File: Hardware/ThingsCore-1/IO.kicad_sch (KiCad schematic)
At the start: 9 parts, among them U7 STM32MP133DAE7, Y1 X322516MLB4SI, Y2 Q13FC13500004

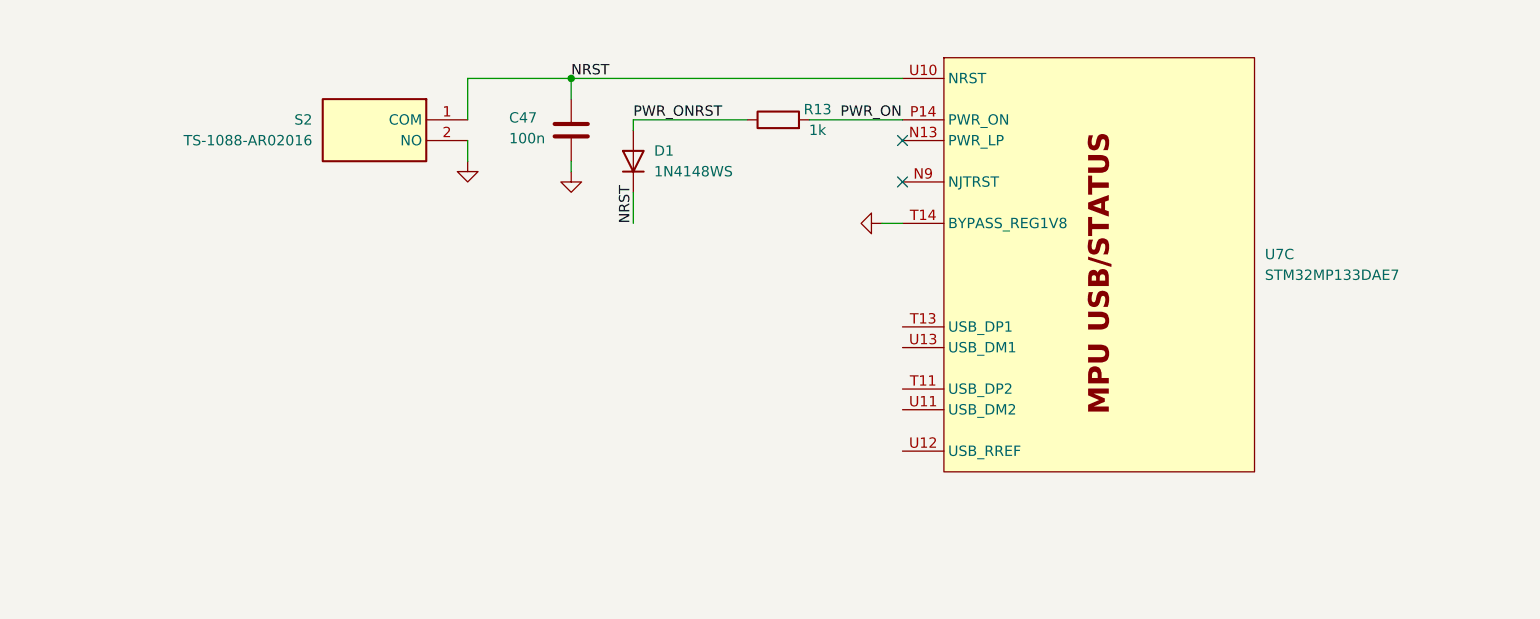
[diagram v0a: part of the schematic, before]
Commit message: ddr3 fanout done
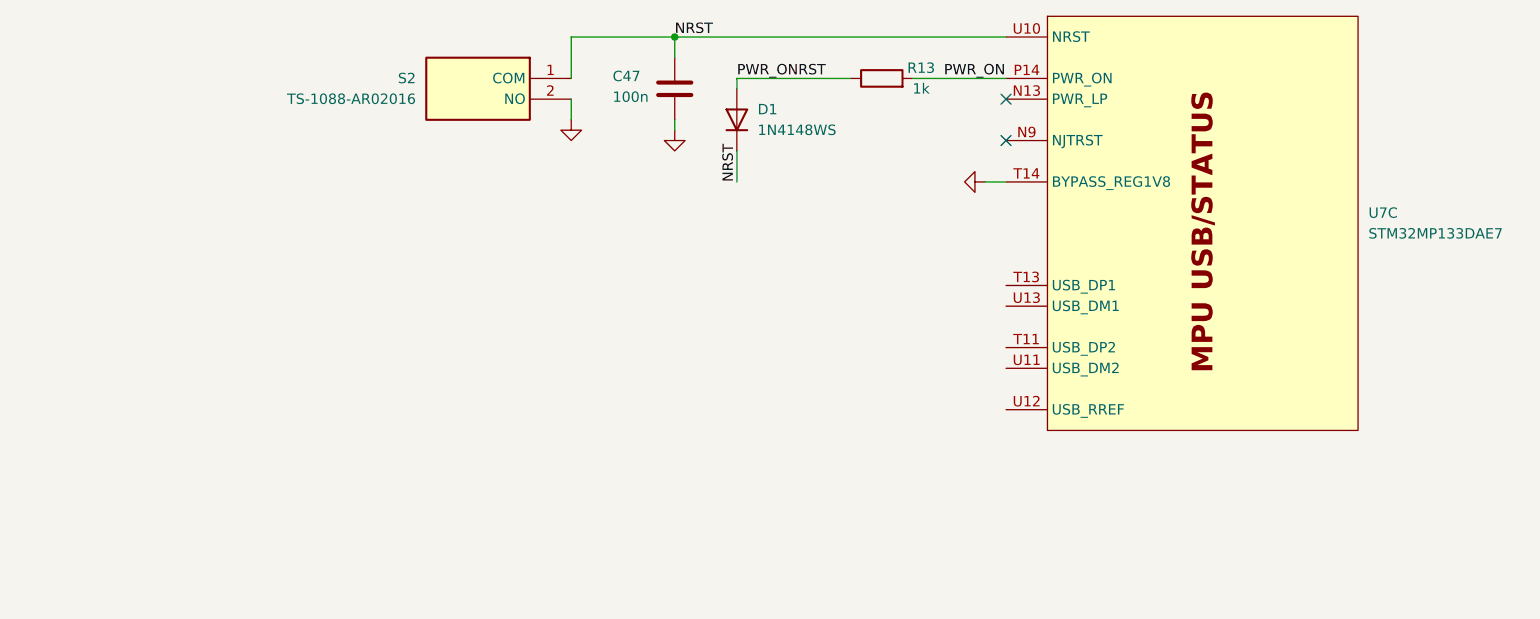
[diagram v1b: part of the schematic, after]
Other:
- moved on the sheet: C47, D1, R13, S2, U7C

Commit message: layout transciever components, pin selection and last components
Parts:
- added C67, C68: 10p, Capacitor_SMD:C_0402_1005Metric, symbol Device:C
- added C69, C70: 15p, Capacitor_SMD:C_0402_1005Metric, symbol Device:C
- added D2: GREEN, LED_SMD:LED_0603_1608Metric, symbol Device:LED
- added D3: RED, LED_SMD:LED_0603_1608Metric, symbol Device:LED
- added D5: BLUE, LED_SMD:LED_0603_1608Metric, symbol Device:LED
- added R20: 33, Resistor_SMD:R_0402_1005Metric, symbol Device:R
- added R32, R33, R34: 1k, Resistor_SMD:R_0402_1005Metric, symbol Device:R
- added R35: 3k, Resistor_SMD:R_0402_1005Metric, symbol Device:R
- added R36: 10k, Resistor_SMD:R_0402_1005Metric, symbol Device:R
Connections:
- net GND: now also S1.2 (NO), U1.2, U1.4, U1.6, Y1.2, Y1.4, C67.1, C68.1, C69.1, C70.1, D2.1 (K), D3.1 (K), D5.1 (K), R35.1
- net USB2_P: now reaches U7.T11 (USB_DP2)
- net USB1_P: now reaches U7.T13 (USB_DP1)
- net USB2_N: now reaches U7.U11 (USB_DM2)
- net USB_RREF: now reaches U7.U12 (USB_RREF)
- net USB_RREF: now also R35.2
- net USB1_N: now reaches U7.U13 (USB_DM1)
- net LSE_OUT: now reaches Y2.1
- net LSE_OUT: now also U7.K2 (PC15), C67.2
- net LSE_IN: now reaches Y2.2
- net LSE_IN: now also U7.K1 (PC14), C68.2
- net HSE_IN: now reaches Y1.1
- net HSE_IN: now also U7.P1 (PH0), C69.2
- net HSE_OUT_C: now reaches Y1.3
- net HSE_OUT_C: now also C70.2, R20.2
- net HSE_OUT: now reaches U7.P2 (PH1)
- net HSE_OUT: now also R20.1
- net USER_SW: now reaches S1.1 (COM)
- net USER_SW: now also R36.1
- net LED2: now reaches U1.1
- net VIN_EDGE: now reaches U1.10
- net VIN_EDGE: now also U1.12, U1.8
- net TXN: now reaches U1.11
- net LED1: now reaches U1.3
- net RXP: now reaches U1.5
- net RXN: now reaches U1.7
- net TXP: now reaches U1.9
- new net: D3.2 (A), R33.1
- new net: D2.2 (A), R34.1
- new net: D5.2 (A), R32.1
- new net 3V3_VDD: R36.2
- new net HB_LD: R33.2
- new net USER_LD: R32.2
- new net VDD_LD: R34.2
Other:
- note added: "BOOT SELECT SW"
- note added: "BUTTONS"
- note added: "LED INDICATORS"
- note added: "USB & SOC STATUS/CONTROL"
- note added: "mPCIe EDGE CONN"
- moved on the sheet: C47, D1, R13, S1, S2, U1, U7C, U7D, U7E, Y1, Y2

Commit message: pin assignment, rst,led, button pins left and checks
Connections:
- net 3V3_VDD: now also U7.T10 (PDR_ON)
- net GND: now also U1.30, U1.39, U1.42, U1.45, U1.51
- net NRST: now also U1.44
- net PWR_ONRST: now also U1.46
- net USB1_N: now also U1.49
- net USB1_P: now also U1.47
- net USB2_N: now also U1.41
- net USB2_P: now also U1.43
- net MMC2_CMD: now reaches U7.A14 (PG6)
- net QSPI1_D1: now reaches U7.B6 (PE9)
- net MMC2_D4: now reaches U7.C13 (PF0)
- net MMC2_CLK: now reaches U7.D13 (PE3)
- net ETH_MDC: now reaches U7.F2 (PG5)
- net ETH_TX_EN: now reaches U7.G2 (PF6)
- net QSPI1_CLK: now reaches U7.G3 (PF10)
- net ETH_~{INT}: now reaches U7.G4 (PG15)
- net ETH_~{INT}: now also U7.G5 (PF8)
- net ETH_REF_CLK: now reaches U7.H1 (PH11)
- net ETH_RX_D1: now reaches U7.L1 (PE2)
- net ETH_RX_D0: now reaches U7.L2 (PF4)
- net ETH_TX_D0: now reaches U7.M1 (PF7)
- net ETH_TX_D1: now reaches U7.M3 (PG11)
- net BOOT1: now reaches U7.P12 (PI5)
- net BOOT1: now also U1.50
- net DBG_JTCK: now reaches U7.P4 (PF14)
- net DBG_JTCK: now also U1.34
- net DBG_JTMS: now reaches U7.R10 (PF15)
- net DBG_JTMS: now also U1.40
- net BOOT2: now reaches U7.R12 (PI6)
- net BOOT2: now also U1.52
- net DBG_JTDO: now reaches U7.R14 (PH5)
- net DBG_JTDO: now also U1.38
- net DBG_JTDI: now reaches U7.T15 (PH4)
- net DBG_JTDI: now also U1.36
- net ADC1_IN6: now reaches U7.T4 (PF12)
- net ADC1_IN6: now also U1.20
- net BOOT0: now reaches U7.U14 (PI4)
- net BOOT0: now also U1.48
- net MMC2_D7: now reaches U7.A11 (PC7)
- net MMC2_D5: now reaches U7.A12 (PB9)
- net MMC2_D0: now reaches U7.A13 (PB14)
- net MMC1_CMD: now reaches U7.A15 (PD2)
- net MMC1_D1: now reaches U7.A16 (PC9)
- net QSPI1_D0: now reaches U7.A6 (PD5)
- net MMC2_D6: now reaches U7.B11 (PC6)
- net MMC2_D1: now reaches U7.B12 (PB15)
- net MMC2_D3: now reaches U7.B13 (PB4)
- net MMC1_D2: now reaches U7.B14 (PC10)
- net MMC1_CLK: now reaches U7.B15 (PC12)
- net ETH_MDIO: now reaches U7.C1 (PB6)
- net MMC2_D2: now reaches U7.C11 (PB3)
- net MMC1_D3: now reaches U7.C14 (PC11)
- net QSPI1_D3: now reaches U7.C7 (PD15)
- net MMC1_D0: now reaches U7.D14 (PC8)
- net QSPI1_~{CS}: now reaches U7.D5 (PD1)
- net QSPI1_D2: now reaches U7.E2 (PD11)
- net ETH_CRS_DV: now reaches U7.E3 (PA12)
- net ADC2_IN3: now reaches U7.R4 (PA1)
- net ADC2_IN3: now also U1.18
- net ADC2_IN0: now reaches U7.T3 (PC0)
- net ADC2_IN0: now also U1.22
- net ADC1_IN13: now reaches U7.T5 (PC3)
- net ADC1_IN13: now also U1.24
- net ADC1_IN16: now reaches U7.U2 (PA7)
- net ADC1_IN16: now also U1.28
- net ADC2_IN7: now reaches U7.U3 (PA0)
- net ADC2_IN7: now also U1.26
- net VBAT: now reaches U1.32
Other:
- note added: "SP1 | I2S1 PINMUX"
- note added: "WAKEUP"
- note removed: "BOOT SELECT SW"
- moved on the sheet: C47, C67, C68, D1, R13, R35, U1, U7C, Y2

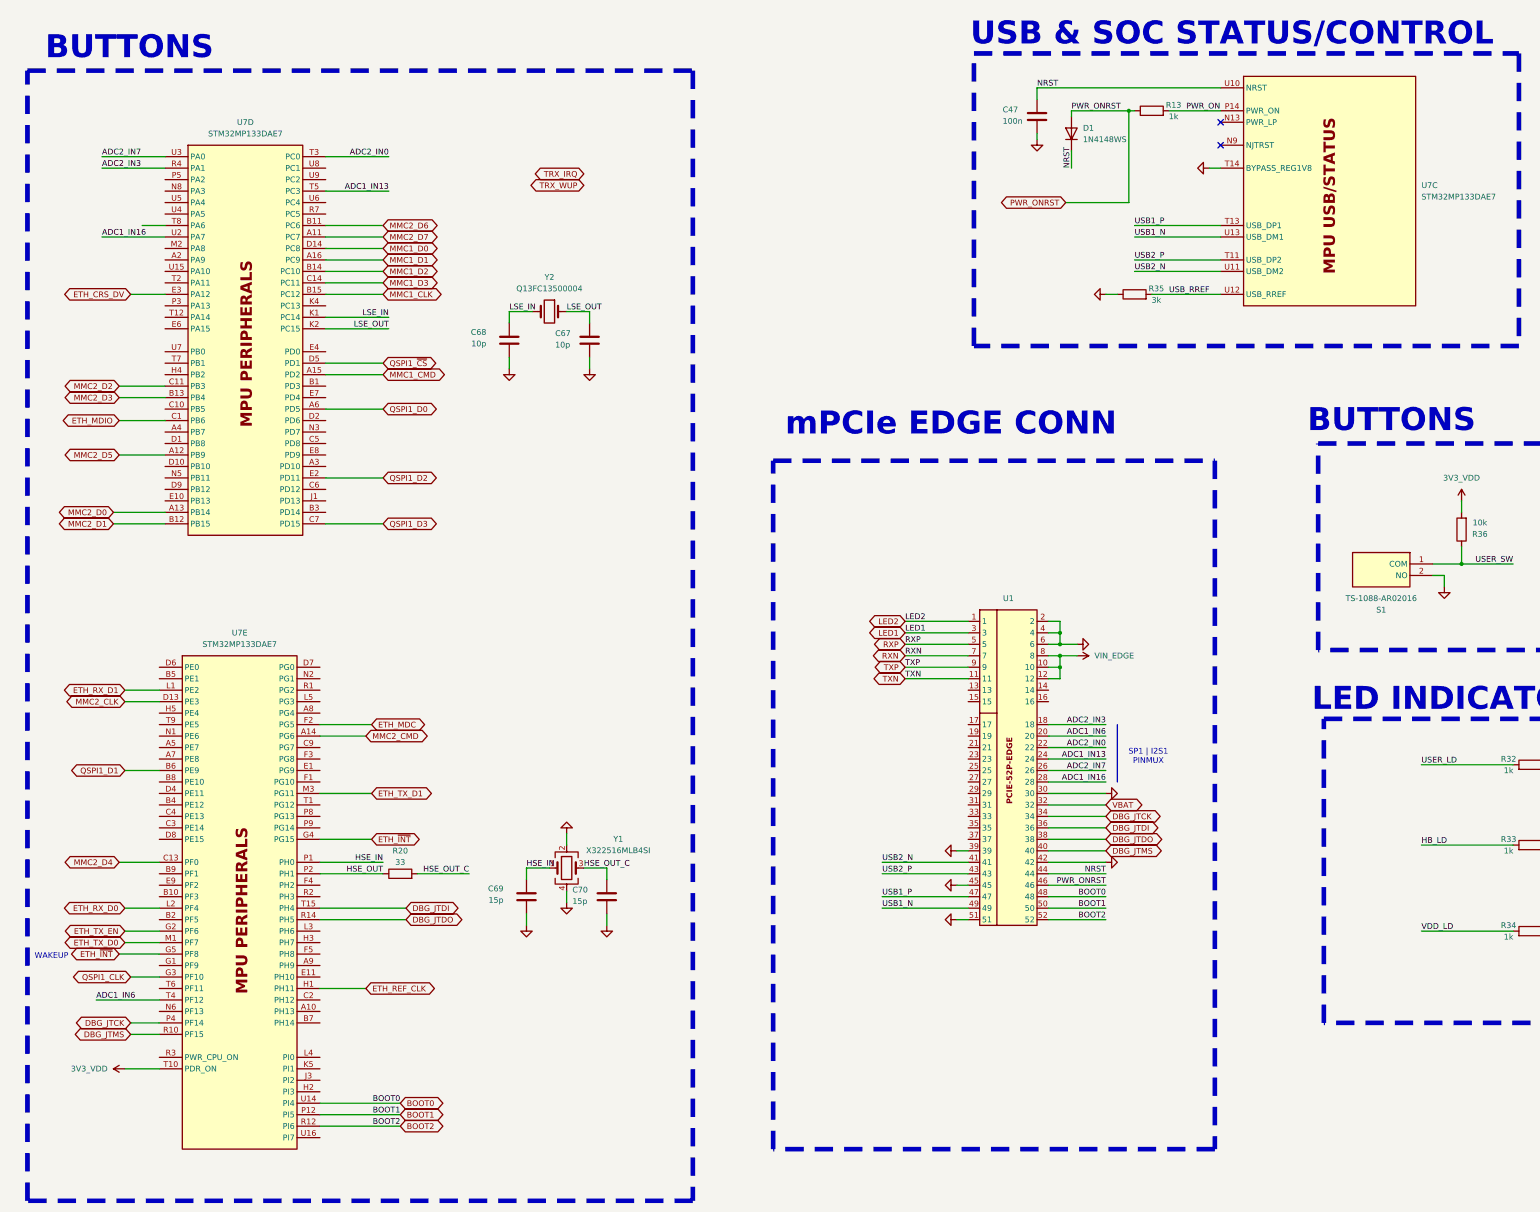
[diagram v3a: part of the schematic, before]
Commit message: checks left and feedback resistors for switchers
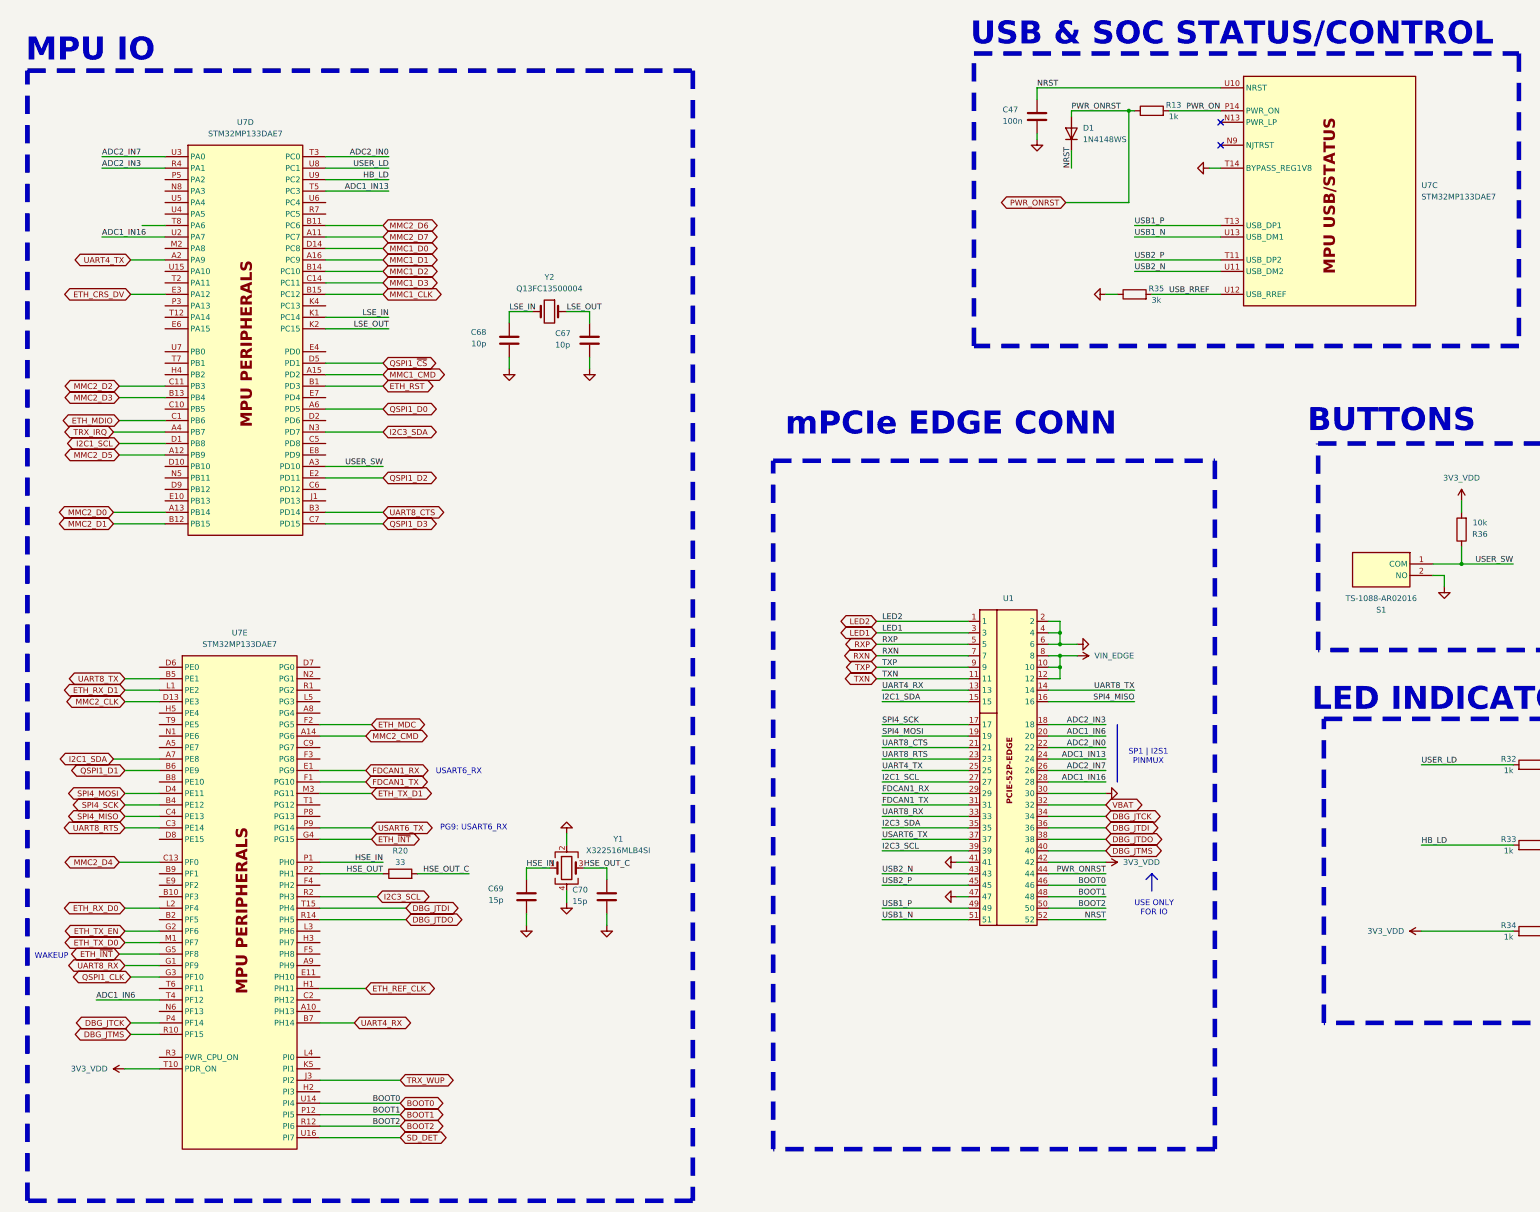
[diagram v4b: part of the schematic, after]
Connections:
- net VDD_LD is gone; now on net 3V3_VDD: R34.2
- net 3V3_VDD: now also U1.42
- net BOOT0: now also U1.46; no longer U1.48
- net BOOT1: now also U1.48; no longer U1.50
- net BOOT2: now also U1.50; no longer U1.52
- net GND: now also U1.41, U1.47; no longer U1.39, U1.42, U1.45, U1.51
- net HB_LD: now also U7.U9 (PC2)
- net NRST: now also U1.52; no longer U1.44
- net PWR_ONRST: now also U1.44; no longer U1.46
- net TRX_IRQ: now also U7.A4 (PB7)
- net TRX_WUP: now also U7.J3 (PI2)
- net USB1_N: now also U1.51; no longer U1.49
- net USB1_P: now also U1.49; no longer U1.47
- net USB2_N: now also U1.43; no longer U1.41
- net USB2_P: now also U1.45; no longer U1.43
- net USER_LD: now also U7.U8 (PC1)
- net USER_SW: now also U7.A3 (PD10)
- net I2C1_SDA: now reaches U7.A7 (PE8)
- net I2C1_SDA: now also U1.15
- net SPI4_SCK: now reaches U7.B4 (PE12)
- net SPI4_SCK: now also U1.17
- net UART8_TX: now reaches U7.B5 (PE1)
- net UART8_TX: now also U1.14
- net UART4_RX: now reaches U7.B7 (PH14)
- net UART4_RX: now also U1.13
- net UART8_RTS: now reaches U7.C3 (PE14)
- net UART8_RTS: now also U1.23
- net SPI4_MISO: now reaches U7.C4 (PE13)
- net SPI4_MISO: now also U1.16
- net SPI4_MOSI: now reaches U7.D4 (PE11)
- net SPI4_MOSI: now also U1.19
- net FDCAN1_RX: now reaches U7.E1 (PG9)
- net FDCAN1_RX: now also U1.29
- net FDCAN1_TX: now reaches U7.F1 (PG10)
- net FDCAN1_TX: now also U1.31
- net UART8_RX: now reaches U7.G1 (PF9)
- net UART8_RX: now also U1.33
- net USART6_TX: now reaches U7.P9 (PG14)
- net USART6_TX: now also U1.37
- net I2C3_SCL: now reaches U7.R2 (PH3)
- net I2C3_SCL: now also U1.39
- net SD_DET: now reaches U7.U16 (PI7)
- net UART4_TX: now reaches U7.A2 (PA9)
- net UART4_TX: now also U1.25
- net ETH_RST: now reaches U7.B1 (PD3)
- net UART8_CTS: now reaches U7.B3 (PD14)
- net UART8_CTS: now also U1.21
- net I2C1_SCL: now reaches U7.D1 (PB8)
- net I2C1_SCL: now also U1.27
- net I2C3_SDA: now reaches U7.N3 (PD7)
- net I2C3_SDA: now also U1.35
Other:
- note added: "MPU IO"
- note added: "PG9: USART6_RX"
- note added: "USART6_RX"
- note added: "USE ONLY FOR IO"
